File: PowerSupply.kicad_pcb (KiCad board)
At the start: 2 copper layers, 105 x 200 mm, 51 parts, among them J1 Barrel_Jack, J2 PowerHeader, M1 MouseBites, M2 MouseBites, M3 MouseBites, M4 MouseBites, SW1 SW_SPST, U1 LM7805_TO220, U2 LM7812_TO220, U3 LM7912_TO220

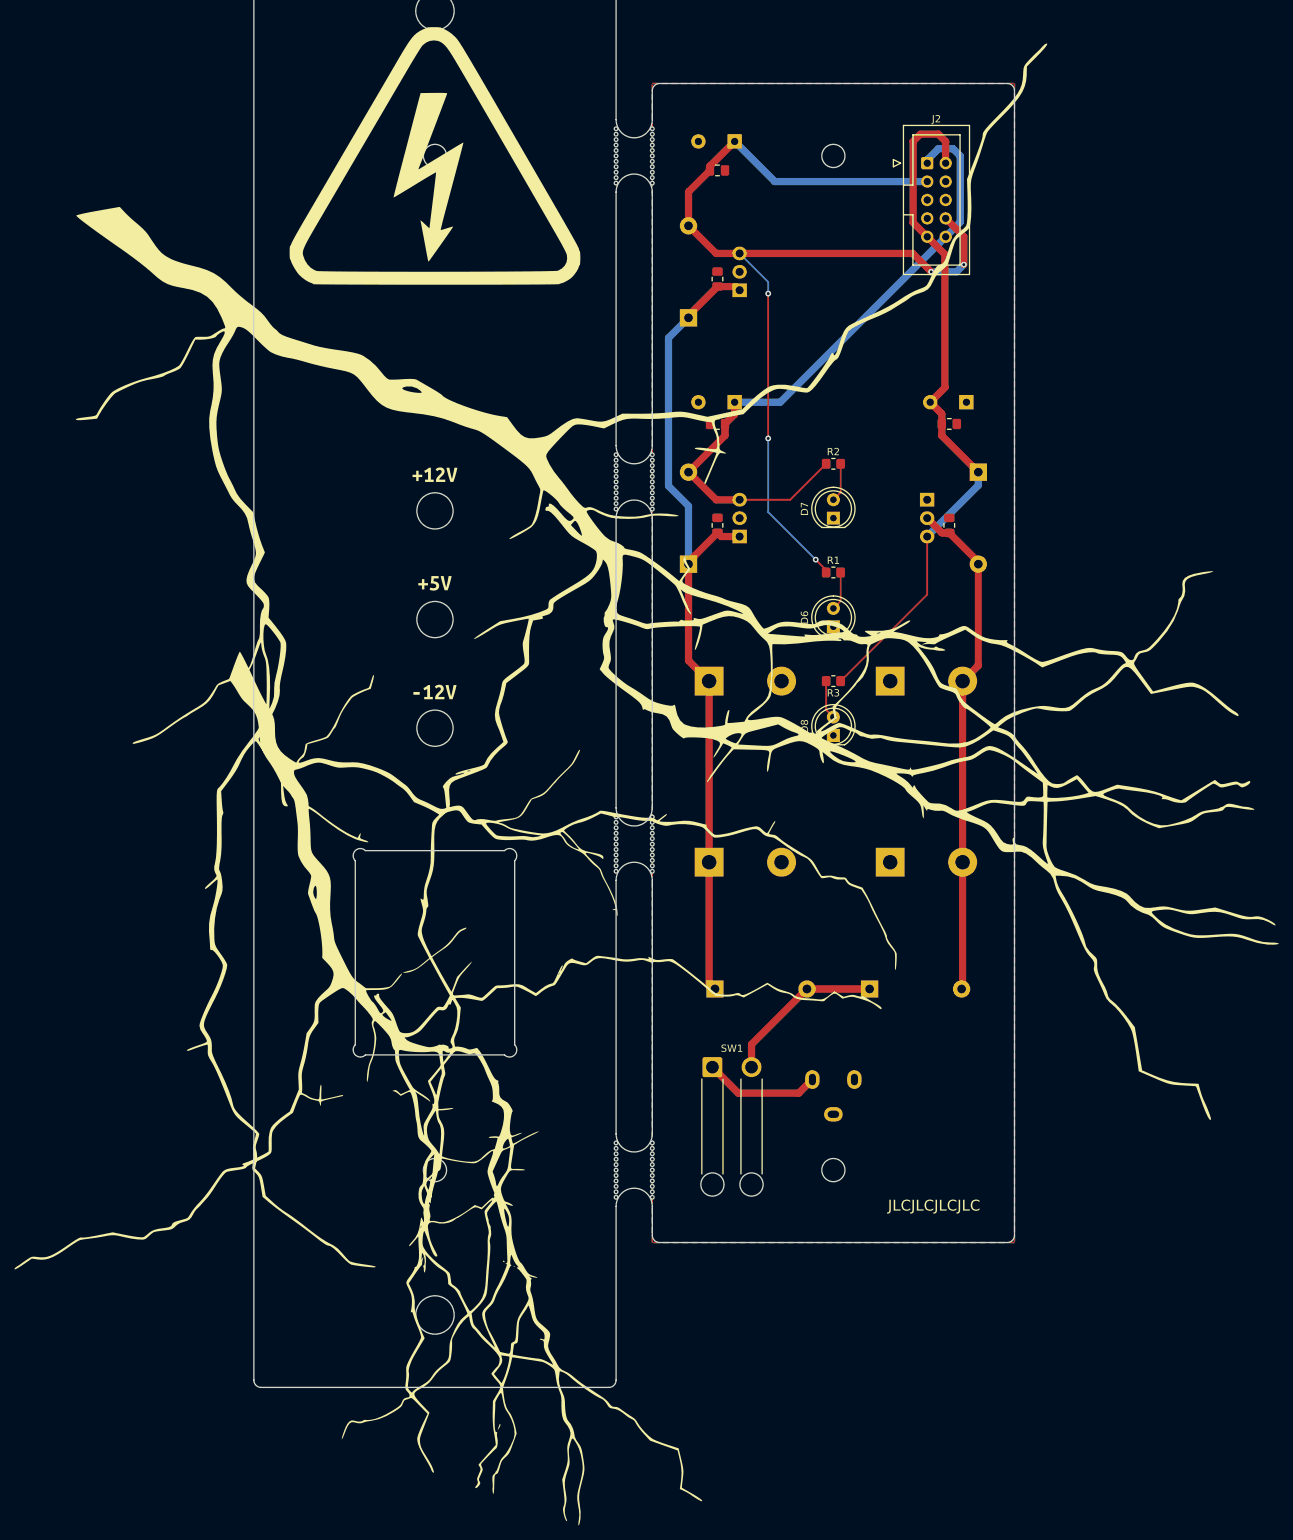
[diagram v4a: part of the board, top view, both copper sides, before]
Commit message: Preliminary design on rework
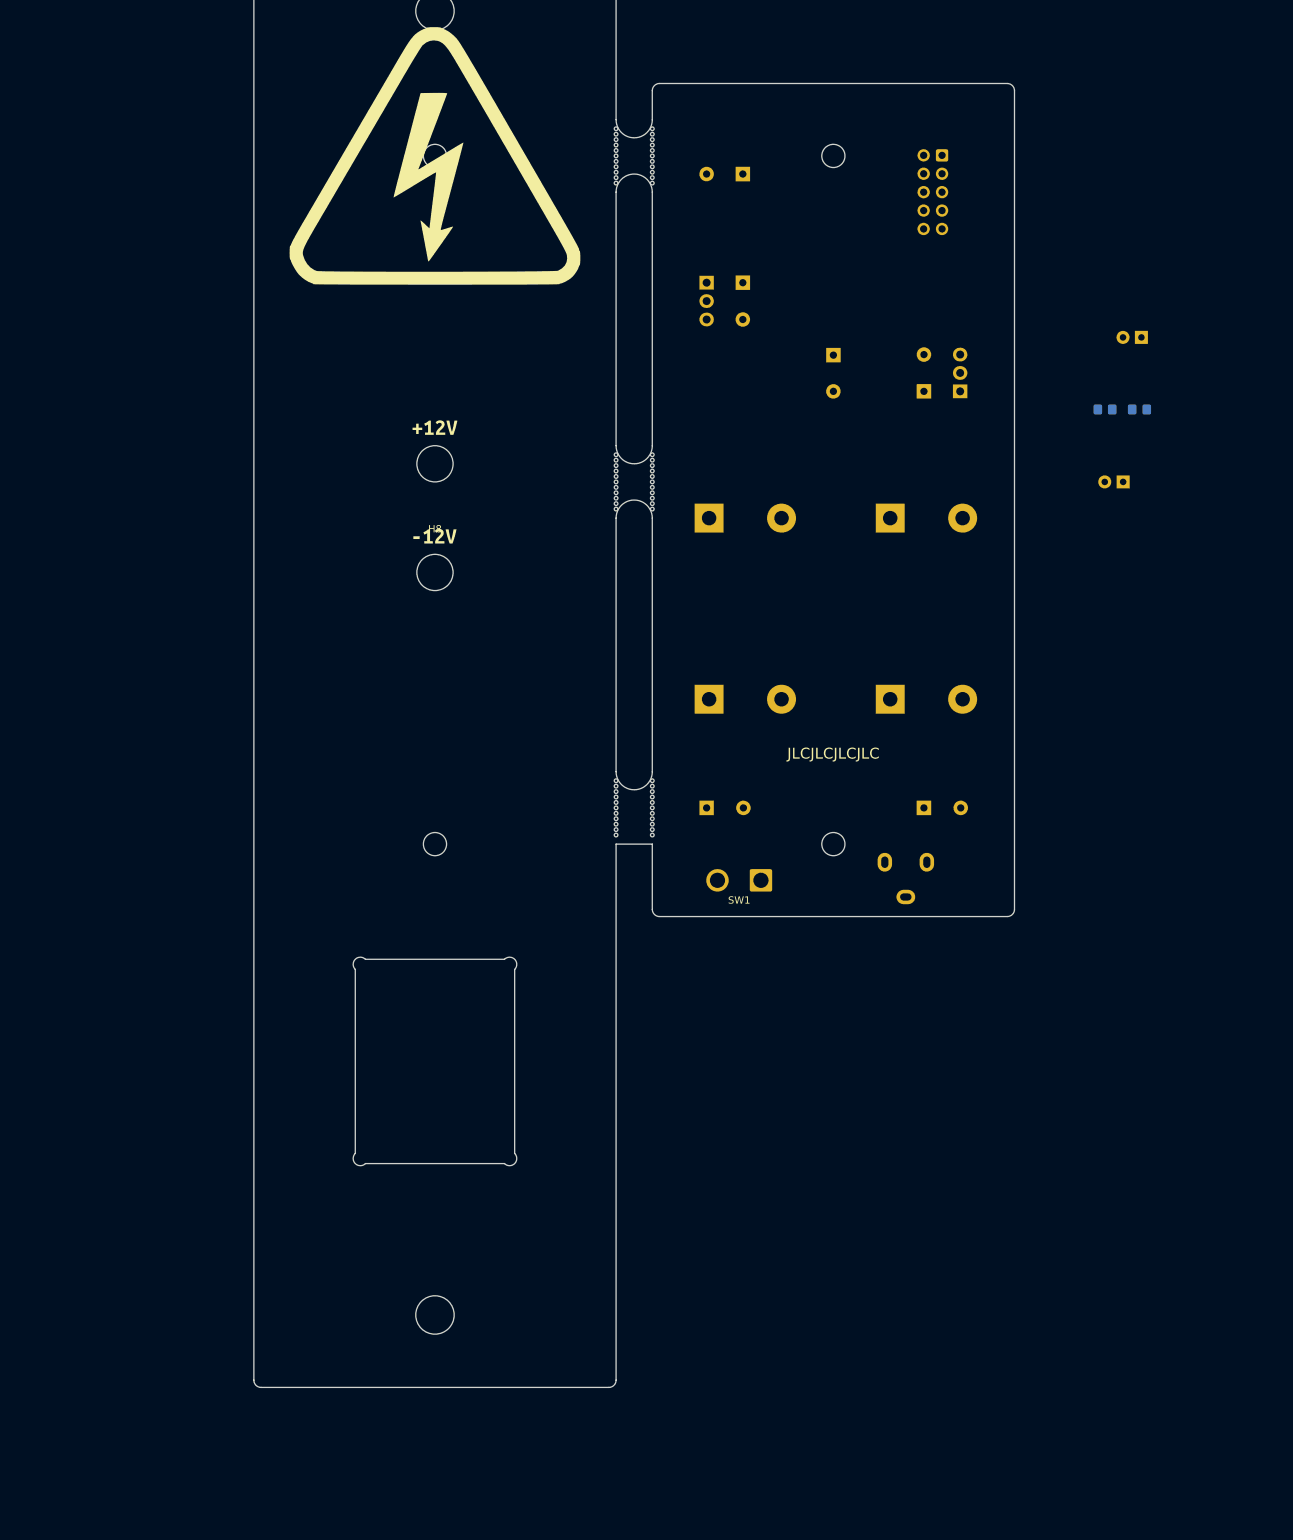
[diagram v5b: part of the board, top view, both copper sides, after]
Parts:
- removed C10, C7, C8, C9: 1uF, Capacitor_SMD:C_0805_2012Metric_Pad1.18x1.45mm_HandSolder
- removed C11, C12, C13: 470uF, Capacitor_THT:CP_Radial_D10.0mm_P5.00mm
- removed D7: 12V LED, LED_THT:LED_D5.0mm
- removed D8: -12V LED, LED_THT:LED_D5.0mm
- removed the G*** at (143.0, 139.8)
- removed the G*** at (113.9, 199.8)
- removed the G*** at (168.4, 147.1)
- removed the H6 at (110.0, 149.0)
- removed the M1 at (137.5, 210.0)
- removed R3: 150R, Resistor_SMD:R_0805_2012Metric_Pad1.20x1.40mm_HandSolder
- removed U3: LM7912_TO220, Package_TO_SOT_THT:TO-220-3_Vertical
- removed kibuzzard-61F37DAA: G***, kibuzzard-61F37DAA
- C5, C6: value 1uF -> 470uF; footprint Capacitor_SMD:C_0805_2012Metric_Pad1.18x1.45mm_HandSolder -> Capacitor_THT:CP_Radial_D10.0mm_P5.00mm; moved to B.Cu
- D1, D2, D3, D4: footprint Diode_THT:D_DO-15_P12.70mm_Horizontal -> Diode_THT:D_T-1_P5.08mm_Horizontal
- D5: value 1N4002 -> 12V LED; footprint Diode_THT:D_DO-15_P12.70mm_Horizontal -> LED_THT:LED_D5.0mm
- D6: value 5V LED -> -12V LED; moved to B.Cu
- J2, R1, R2: moved to B.Cu
- SW1: footprint Connector_Wire:SolderWire-1sqmm_1x02_P5.4mm_D1.4mm_OD2.7mm_Relief -> Connector_Wire:SolderWire-1.5sqmm_1x02_P6mm_D1.7mm_OD3mm
- U1: value LM7805_TO220 -> LM7812_TO220
- U2: value LM7812_TO220 -> LM7912_TO220
- moved C4 47.5 mm to (172.8, 120.0)
- moved C1 47.5 mm to (147.8, 120.0)
- moved H5 45.0 mm to (165.0, 165.0)
- moved H7 45.0 mm to (110.0, 165.0)
- moved D6 44.7 mm to (205.0, 115.0), turned to 180 degrees
- moved R1 43.7 mm to (202.5, 105.0), turned to 180 degrees
- moved R2 42.9 mm to (207.2, 105.0), turned to 180 degrees
- moved D4 40.3 mm to (177.5, 102.5)
- moved U2 36.4 mm to (182.5, 102.5)
- moved J1 31.6 mm to (175.0, 167.5)
- moved D5 29.2 mm to (207.5, 95.0), turned to 180 degrees
- moved C6 28.4 mm to (165.0, 97.5), turned to -90 degrees
- moved SW1 26.6 mm to (155.0, 170.0), turned to 180 degrees
- moved D2 26.1 mm to (177.5, 160.0)
- moved D1 25.0 mm to (147.5, 160.0)
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- renumbered H9 to H2, H10 to H3, H2 to H4, H3 to H5, H4 to H6, H5 to H7, H7 to H9, M2 to M1, M3 to M2, M4 to M3
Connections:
- C5 pad 1: Net-(C1-Pad1) -> +12V
- C6 pad 1: Net-(C1-Pad1) -> GND
- C6 pad 2: GND -> -12V
- D3 pad 2: +5V -> +12V
- D4 pad 1: Net-(C1-Pad1) -> -12V
- D4 pad 2: +12V -> Net-(C2-Pad2)
- D5 pad 1: -12V -> GND
- D5 pad 2: Net-(C2-Pad2) -> Net-(D5-Pad2)
- J2 pad 1: +12V -> -12V
- J2 pad 3: +5V -> GND
- J2 pad 8: +5V -> GND
- J2 pad 9: -12V -> +12V
- R1 pad 1: +5V -> +12V
- R1 pad 2: Net-(D6-Pad2) -> Net-(D5-Pad2)
- R2 pad 1: +12V -> -12V
- R2 pad 2: Net-(D7-Pad2) -> Net-(D6-Pad2)
- U1 pad 3: +5V -> +12V
- U2 pad 1: Net-(C1-Pad1) -> GND
- U2 pad 2: GND -> Net-(C2-Pad2)
- U2 pad 3: +12V -> -12V
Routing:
- net +5V: track 140.6 -> 0.00 mm, vias 5 -> 0
- net Net-(C1-Pad1): track 114.9 -> 0.00 mm
- net -12V: track 96.1 -> 0.00 mm
- net +12V: track 91.6 -> 0.00 mm
- net Net-(C2-Pad2): track 69.5 -> 0.00 mm
- net Net-(D1-Pad2): track 22.6 -> 0.00 mm
- net Net-(J1-Pad1): track 16.1 -> 0.00 mm
- net Net-(D8-Pad2): track 5.37 -> 0.00 mm
- net Net-(D6-Pad2): track 5.37 -> 0.00 mm
- net Net-(D7-Pad2): track 5.37 -> 0.00 mm
- removed copper zone on B.Cu, net GND
- removed copper zone on F.Cu, net GND
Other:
- outline, holes or cut-outs redrawn

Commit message: Production v2
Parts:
- added C5: 0.1uF, Capacitor_SMD_Handsoldering_AKL:C_0805_2012Metric_Pad1.18x1.45mm, F.Cu at (183.0, 97.0)
- added C6: 0.1uF, Capacitor_SMD_Handsoldering_AKL:C_0805_2012Metric_Pad1.18x1.45mm, F.Cu at (156.5, 90.5)
- added C7: 0.1uF, Capacitor_SMD_Handsoldering_AKL:C_0805_2012Metric_Pad1.18x1.45mm, F.Cu at (183.0, 86.0)
- added C8: 0.1uF, Capacitor_SMD_Handsoldering_AKL:C_0805_2012Metric_Pad1.18x1.45mm, F.Cu at (154.0, 86.0)
- added D7: 1N4002, Diode_THT:D_T-1_P5.08mm_Horizontal, B.Cu at (175.0, 89.0)
- added D8: 1N4002, Diode_THT:D_T-1_P5.08mm_Horizontal, B.Cu at (144.0, 94.0)
- added R1: 1R 1W, Resistor_THT_AKL:R_Axial_DIN0414_L11.9mm_D4.5mm_P15.24mm_Horizontal, B.Cu at (186.5, 137.1)
- added R2: 1R 1W, Resistor_THT_AKL:R_Axial_DIN0414_L11.9mm_D4.5mm_P15.24mm_Horizontal, B.Cu at (143.5, 137.1)
- D5, D6: moved to F.Cu
- R3: renamed from R1; footprint Resistor_SMD:R_0805_2012Metric_Pad1.20x1.40mm_HandSolder -> Resistor_SMD_AKL:R_0805_2012Metric_Pad1.20x1.40mm; moved to F.Cu
- R4: renamed from R2; footprint Resistor_SMD:R_0805_2012Metric_Pad1.20x1.40mm_HandSolder -> Resistor_SMD_AKL:R_0805_2012Metric_Pad1.20x1.40mm; moved to F.Cu
- U1, U2: footprint Package_TO_SOT_THT:TO-220-3_Vertical -> Package_TO_SOT_THT_AKL:TO-220-3_Vertical
- moved D5 51.0 mm to (165.0, 123.3), turned to 90 degrees
- moved R4 50.1 mm to (165.0, 132.0), turned to -90 degrees
- moved C3 48.2 mm to (183.0, 112.0), turned to 180 degrees
- moved D6 46.5 mm to (165.0, 138.8), turned to 90 degrees
- moved C1 44.3 mm to (183.0, 147.0), turned to 180 degrees
- moved R3 39.1 mm to (165.0, 116.0), turned to -90 degrees
- moved U1 37.1 mm to (184.0, 94.0), turned to 90 degrees
- moved D1 33.0 mm to (180.5, 160.5), turned to 180 degrees
- moved D4 32.0 mm to (148.5, 89.0), turned to -90 degrees
- moved U2 30.7 mm to (153.0, 94.0)
- moved D3 27.8 mm to (179.5, 94.0), turned to 90 degrees
- moved C10 27.5 mm to (146.1, 77.5), turned to 0 degrees
- moved D2 23.0 mm to (154.5, 160.5), turned to 180 degrees
- moved C9 20.7 mm to (165.0, 89.0), turned to 90 degrees
- moved C4 17.7 mm to (157.0, 112.0), turned to 180 degrees
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- renumbered C6 to C10, C5 to C9, H9 to H6, H8 to H7, H6 to H8, H7 to H9
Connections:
- C3 pad 1: Net-(C1-Pad1) -> Net-(C3-Pad1)
- C4 pad 2: Net-(C2-Pad2) -> Net-(C4-Pad2)
- D3 pad 1: Net-(C1-Pad1) -> Net-(C3-Pad1)
- D4 pad 2: Net-(C2-Pad2) -> Net-(C4-Pad2)
- U1 pad 1: Net-(C1-Pad1) -> Net-(C3-Pad1)
- U2 pad 2: Net-(C2-Pad2) -> Net-(C4-Pad2)
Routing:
- net -12V: track 0.00 -> 103.0 mm, vias 0 -> 1
- net +12V: track 0.00 -> 59.9 mm
- net Net-(C4-Pad2): track 0.00 -> 39.0 mm
- net Net-(C3-Pad1): track 0.00 -> 34.2 mm
- net Net-(D1-Pad2): track 0.00 -> 33.8 mm
- net Net-(C2-Pad2): track 0.00 -> 25.8 mm
- net Net-(C1-Pad1): track 0.00 -> 25.8 mm
- net Net-(J1-Pad1): track 0.00 -> 17.3 mm
- net Net-(D6-Pad2): track 0.00 -> 3.74 mm
- net Net-(D5-Pad2): track 0.00 -> 3.73 mm
- added copper zone on B.Cu, net GND
- added copper zone on F.Cu, net GND
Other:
- board text added: "POWER SWITCH"
